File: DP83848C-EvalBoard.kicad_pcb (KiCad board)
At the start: 4 copper layers, 165 parts, among them J1 Conn_02x08_Odd_Even, J10 RJ45_LED_Shielded, J11 USB_C_Receptacle_USB2.0, J12 Conn_02x05_Odd_Even, J2 Conn_02x08_Odd_Even, J3 Conn_02x04_Odd_Even, J4 Conn_01x04, J5 Conn_01x04, J6 Conn_02x04_Odd_Even, J7 Conn_02x04_Odd_Even, J8 Conn_02x04_Odd_Even, J9 Conn_01x02, Q1 AO3401A, Q2 AO3400A, Q3 AO3401A, SW1 SW_Push, T1 H1102NL, U1 AMS1117-3.3, U2 DP83848C, U3 STM32F407VGTx, U4 USBLC6-2SC6, X1 50MHz, Y1 25MHz

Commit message: Test...
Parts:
- added R98: 0, Resistor_SMD:R_1206_3216Metric, F.Cu at (157.5, 40.6)
- added R99: 0, Resistor_SMD:R_1206_3216Metric, F.Cu at (157.5, 43.9)
- moved C14 10.4 mm to (139.7, 73.2), turned to 270 degrees
- moved R30 9.80 mm to (141.2, 78.2), turned to 270 degrees
- moved R25 9.51 mm to (141.2, 80.3), turned to 90 degrees
- moved C11 8.63 mm to (142.2, 78.2), turned to 90 degrees
- moved R26 8.29 mm to (142.2, 80.3), turned to 270 degrees
- moved R31 6.71 mm to (144.3, 78.2), turned to 270 degrees
- moved C12 5.85 mm to (143.3, 78.2), turned to 90 degrees
- moved R27 5.80 mm to (143.3, 80.3), turned to 90 degrees
- moved R28 5.39 mm to (144.3, 80.3), turned to 270 degrees
- moved C16 4.31 mm to (131.3, 57.7)
- moved J10 4.31 mm to (147.8, 51.3)
- moved R38 4.31 mm to (133.9, 61.5)
- moved R39 4.31 mm to (133.9, 60.2)
- moved R41 4.31 mm to (133.9, 57.7)
- moved T1 4.31 mm to (142.7, 66.5)
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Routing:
- net /PHY/RX+: track 17.7 -> 0.00 mm
- net /PHY/TX+: track 15.6 -> 0.00 mm
- net Net-(J10-Pad4): track 14.8 -> 0.00 mm
- net /PHY/RXC: track 14.2 -> 0.00 mm
- net /PHY/RX-: track 24.3 -> 11.8 mm
- net /PHY/TX-: track 10.8 -> 0.00 mm
- net /PHY/TXC: track 9.61 -> 0.00 mm
- net Net-(J10-Pad7): track 9.22 -> 0.00 mm
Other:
- board outline added: 105 x 150 mm
- net class Default: trace_width 0.25 -> 0.2; via_dia 0.8 -> 0.6; via_drill 0.4 -> 0.3

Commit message: Placement
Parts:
- added J13: Conn_01x04, Connector_PinHeader_2.54mm:PinHeader_1x04_P2.54mm_Vertical, F.Cu at (45.0, 132.2)
- added J14: Conn_02x04_Odd_Even, Connector_PinHeader_2.54mm:PinHeader_2x04_P2.54mm_Vertical, F.Cu at (121.9, 128.0)
- added R100: 33, Resistor_SMD:R_0805_2012Metric, F.Cu at (118.0, 128.0)
- added R101: 33, Resistor_SMD:R_0805_2012Metric, F.Cu at (118.0, 130.5)
- added R102: 33, Resistor_SMD:R_0805_2012Metric, F.Cu at (118.0, 133.0)
- added R103: 33, Resistor_SMD:R_0805_2012Metric, F.Cu at (118.0, 135.5)
- C10, C4: footprint Capacitor_SMD:C_0402_1005Metric -> Capacitor_Tantalum_SMD:CP_EIA-3216-18_Kemet-A
- R30, R31: value 0 -> 33; footprint Resistor_SMD:R_0402_1005Metric -> Resistor_SMD:R_0805_2012Metric
- R64, R65, R66, R67, R68, R69, R70, R71, R72, R73, R74, R75, R76, R77, R78, R79, R80, R81, R82, R83, R84, R85, R86, R87, R88, R89, R90, R91, R92, R93, R94, R95, R96, R97: footprint Resistor_SMD:R_1206_3216Metric -> Resistor_SMD:R_0805_2012Metric
- moved J7 202.2 mm to (47.9, 123.6), turned to 180 degrees
- moved R92 193.0 mm to (53.0, 123.6)
- moved R93 190.9 mm to (53.0, 121.1)
- moved R94 189.0 mm to (53.0, 118.5)
- moved R80 187.2 mm to (42.0, 101.5)
- moved R81 187.2 mm to (42.0, 104.1)
- moved R82 187.2 mm to (42.0, 106.6)
- moved R83 187.2 mm to (42.0, 109.1)
- moved R95 187.2 mm to (53.0, 116.0), turned to 0 degrees
- moved J2 186.8 mm to (46.9, 74.7)
- moved R72 186.8 mm to (41.8, 74.7)
- moved R73 186.8 mm to (41.8, 77.2)
- moved R74 186.8 mm to (41.8, 79.8)
- moved R75 186.8 mm to (41.8, 82.3)
- moved R76 186.8 mm to (41.8, 84.9)
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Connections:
- C11 pad 1: Net-(C11-Pad1) -> +3V3
- C12 pad 1: Net-(C12-Pad1) -> +3V3
- R25 pad 2: Net-(C11-Pad1) -> +3V3
- R26 pad 1: Net-(C11-Pad1) -> +3V3
- R27 pad 2: Net-(C12-Pad1) -> +3V3
- R28 pad 1: Net-(C12-Pad1) -> +3V3
- R30 pad 1: +3V3 -> /MCU/USART3_RX
- R30 pad 2: Net-(C11-Pad1) -> Net-(J13-Pad2)
- R31 pad 1: +3V3 -> /MCU/USART3_TX
- R31 pad 2: Net-(C12-Pad1) -> Net-(J13-Pad3)
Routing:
- net /PHY/TD-: track 0.00 -> 15.9 mm
- net /PHY/TD+: track 0.00 -> 15.8 mm
- net /PHY/RD-: track 0.00 -> 15.3 mm
- net /PHY/RD+: track 0.00 -> 14.2 mm
- net /PHY/PFB: track 0.00 -> 13.6 mm, vias 0 -> 2
- net /PHY/RX-: track 11.8 -> 0.00 mm
- net +3V3: track 0.00 -> 7.93 mm, vias 0 -> 7
- net Net-(R23-Pad2): track 0.00 -> 7.56 mm, vias 0 -> 2
- net GND: track 0.00 -> 5.69 mm, vias 0 -> 7
- net Net-(R24-Pad2): track 0.00 -> 5.44 mm, vias 0 -> 2
- net Net-(R19-Pad1): track 0.00 -> 4.58 mm
- net Net-(R16-Pad1): track 0.00 -> 4.47 mm
- net Net-(R18-Pad1): track 0.00 -> 4.43 mm
- net Net-(R14-Pad1): track 0.00 -> 4.35 mm
- net Net-(R10-Pad1): track 0.00 -> 4.24 mm
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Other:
- board size 105 x 150 mm -> 100 x 100 mm
- net class Default: clearance 0.2 -> 0.15; trace_width 0.2 -> 0.15
- rule trace_clearance: 0.2 -> 0.15
- rule trace_min: 0.2 -> 0.1
- rule via_min_drill: 0.3 -> 0.25
- rule via_min_size: 0.4 -> 0.5

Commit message: Routing
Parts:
- added C32: 10uF, Capacitor_Tantalum_SMD:CP_EIA-3216-18_Kemet-A, F.Cu at (88.8, 107.5)
- added H1: MountingHole_Pad, MountingHole:MountingHole_3.2mm_M3_Pad_Via, F.Cu at (45.0, 152.0)
- added H2: MountingHole_Pad, MountingHole:MountingHole_3.2mm_M3_Pad_Via, F.Cu at (45.0, 62.0)
- added H3: MountingHole_Pad, MountingHole:MountingHole_3.2mm_M3_Pad_Via, F.Cu at (120.0, 152.0)
- added H4: MountingHole_Pad, MountingHole:MountingHole_3.2mm_M3_Pad_Via, F.Cu at (120.0, 62.0)
- C1: footprint Capacitor_SMD:C_0402_1005Metric -> Capacitor_SMD:C_Elec_6.3x7.7
- C2: value 22uF -> 100uF; footprint Capacitor_SMD:C_0402_1005Metric -> Capacitor_Tantalum_SMD:CP_EIA-3528-15_AVX-H
- J10: footprint Connector_RJ:RJ45_Hanrun_HR911105A -> Connector_RJ:RJ45_Amphenol_RJHSE538X
- J9: footprint Connector_PinHeader_2.54mm:PinHeader_1x02_P2.54mm_Vertical -> ak:Molex_022112022
- R1, R2: footprint Resistor_SMD:R_0402_1005Metric -> Resistor_SMD:R_0603_1608Metric
- R100, R101, R102, R103, R30, R31, R64, R65, R66, R67, R68, R69, R70, R71, R72, R73, R74, R75, R76, R77, R78, R79, R80, R81, R82, R83, R84, R85, R86, R87, R88, R89, R90, R91, R92, R93, R94, R95, R96, R97: footprint Resistor_SMD:R_0805_2012Metric -> Resistor_SMD:R_0603_1608Metric
- moved J13 74.2 mm to (118.1, 144.8), turned to 180 degrees
- moved R30 61.2 mm to (109.2, 145.4), turned to 0 degrees
- moved R31 60.3 mm to (109.2, 139.7), turned to 0 degrees
- moved R56 59.3 mm to (97.0, 103.7)
- moved R54 56.7 mm to (99.2, 103.7)
- moved JP2 50.6 mm to (95.8, 67.0), turned to 0 degrees
- moved R34 50.3 mm to (98.8, 70.2), turned to 180 degrees
- moved R98 49.6 mm to (51.0, 66.0), turned to 180 degrees
- moved R36 46.7 mm to (74.0, 68.5), turned to 90 degrees
- moved R37 45.9 mm to (84.2, 68.5), turned to 90 degrees
- moved R35 45.8 mm to (98.8, 75.2), turned to 180 degrees
- moved J10 45.1 mm to (49.0, 81.0), turned to 90 degrees
- moved R55 45.0 mm to (97.0, 114.0)
- moved JP7 44.9 mm to (99.3, 111.2), turned to 180 degrees
- moved C4 44.1 mm to (92.0, 69.8), turned to 90 degrees
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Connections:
- net /ADC0 renamed /MCU/ADC_IN0
- net /ADC1 renamed /MCU/ADC_IN3
- net /ADC2 renamed /MCU/ADC_IN6
- net /ADC3 renamed /MCU/ADC_IN8
- net /ADC4 renamed /MCU/ADC_IN9
- net /ADC5 renamed /MCU/ADC_IN10
- net /ADC6 renamed /MCU/ADC_IN12
- net /ADC7 renamed /MCU/ADC_IN13
- net /GPIO0 renamed /MCU/GPIO0
- net /GPIO1 renamed /MCU/GPIO1
- net /GPIO2 renamed /MCU/GPIO2
- net /GPIO3 renamed /MCU/GPIO3
- net /GPIO4 renamed /MCU/GPIO4
- net /GPIO5 renamed /MCU/GPIO5
- net /GPIO6 renamed /MCU/GPIO6
- net /GPIO7 renamed /MCU/GPIO7
- net /TMR1 renamed /MCU/TMR_CH1
- net /TMR2 renamed /MCU/TMR_CH2
- net /TMR3 renamed /MCU/TMR_CH3
- net /TMR4 renamed /MCU/TMR_CH4
- net Net-(J1-Pad1) renamed /GPIO0_R
- net Net-(J1-Pad11) renamed /GPIO5_R
- net Net-(J1-Pad13) renamed /GPIO6_R
- net Net-(J1-Pad15) renamed /GPIO7_R
- net Net-(J1-Pad3) renamed /GPIO1_R
- net Net-(J1-Pad5) renamed /GPIO2_R
- net Net-(J1-Pad7) renamed /GPIO3_R
- net Net-(J1-Pad9) renamed /GPIO4_R
- net Net-(J13-Pad2) renamed /USART3_TX_R
- net Net-(J13-Pad3) renamed /USART3_RX_R
- net Net-(J14-Pad1) renamed /SPI3_MISO_R
- net Net-(J14-Pad3) renamed /SPI3_MOSI_R
- net Net-(J14-Pad5) renamed /SPI3_SCK_R
- net Net-(J14-Pad7) renamed /SPI3_NSS_R
- net Net-(J2-Pad1) renamed /ADC0_R
- net Net-(J2-Pad11) renamed /ADC5_R
- net Net-(J2-Pad13) renamed /ADC6_R
- net Net-(J2-Pad15) renamed /ADC7_R
- net Net-(J2-Pad3) renamed /ADC1_R
- net Net-(J2-Pad5) renamed /ADC2_R
- net Net-(J2-Pad7) renamed /ADC3_R
- net Net-(J2-Pad9) renamed /ADC4_R
- net Net-(J3-Pad1) renamed /TMR1_R
- net Net-(J3-Pad3) renamed /TMR2_R
- net Net-(J3-Pad5) renamed /TMR3_R
- net Net-(J3-Pad7) renamed /TMR4_R
- net Net-(J4-Pad2) renamed /USART1_TX_R
- net Net-(J4-Pad3) renamed /USART1_RX_R
- net Net-(J5-Pad2) renamed /USART2_TX_R
- net Net-(J5-Pad3) renamed /USART2_RX_R
- net Net-(J6-Pad1) renamed /SPI1_MISO_R
- net Net-(J6-Pad3) renamed /SPI1_MOSI_R
- net Net-(J6-Pad5) renamed /SPI1_SCK_R
- net Net-(J6-Pad7) renamed /SPI1_NSS
- net Net-(J7-Pad1) renamed /SPI2_MISO_R
- net Net-(J7-Pad3) renamed /SPI2_MOSI_R
- net Net-(J7-Pad5) renamed /SPI2_SCK_R
- net Net-(J7-Pad7) renamed /SPI2_NSS_R
- net Net-(R51-Pad1) renamed /MCU/VREF+
- J8 pad 2: +3V3 -> Net-(J8-Pad2)
- J8 pad 3: Net-(J8-Pad3) -> /I2C1_SCL_R
- J8 pad 4: Net-(J8-Pad4) -> /I2C1_SCL_R
- J8 pad 5: Net-(J8-Pad5) -> /I2C1_SDA_R
- J8 pad 6: Net-(J8-Pad6) -> /I2C1_SDA_R
- J8 pad 8: +3V3 -> Net-(J8-Pad8)
- R1 pad 1: Net-(J8-Pad6) -> +3V3
- R1 pad 2: Net-(J8-Pad5) -> Net-(J8-Pad2)
- R2 pad 1: Net-(J8-Pad4) -> +3V3
- R2 pad 2: Net-(J8-Pad3) -> Net-(J8-Pad8)
- R30 pad 1: /MCU/USART3_RX -> /MCU/USART3_TX
- R31 pad 1: /MCU/USART3_TX -> /MCU/USART3_RX
- R84 pad 1: /USART1_RX -> /MCU/USART1_TX
- R85 pad 1: /USART1_TX -> /MCU/USART1_RX
- R86 pad 1: /USART2_RX -> /MCU/USART2_TX
- R87 pad 1: /USART2_TX -> /MCU/USART2_RX
- R96 pad 1: Net-(J8-Pad3) -> /I2C1_SCL_R
- R96 pad 2: /MCU/I2C1_SDA -> /MCU/I2C1_SCL
- R97 pad 1: Net-(J8-Pad5) -> /I2C1_SDA_R
- R97 pad 2: /MCU/I2C1_SCL -> /MCU/I2C1_SDA
- U3 pad 68: /USART1_TX -> /MCU/USART1_TX
- U3 pad 69: /USART1_RX -> /MCU/USART1_RX
- U3 pad 86: /USART2_TX -> /MCU/USART2_TX
- U3 pad 87: /USART2_RX -> /MCU/USART2_RX
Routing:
- net /MCU/NRST: track 0.00 -> 92.5 mm, vias 0 -> 2
- net /ETH_TX_D1: track 0.00 -> 67.3 mm, vias 0 -> 1
- net /ETH_TX_D0: track 0.00 -> 66.4 mm, vias 0 -> 2
- net /ETH_TX_EN: track 0.00 -> 66.0 mm, vias 0 -> 2
- net /ETH_RXD1: track 0.00 -> 58.2 mm, vias 0 -> 2
- net /ETH_RXD0: track 0.00 -> 56.4 mm, vias 0 -> 2
- net /ETH_CRS_DV: track 0.00 -> 53.8 mm, vias 0 -> 2
- net /MCU/USART2_TX: track 0.00 -> 50.4 mm, vias 0 -> 2
- net /MCU/GPIO6: track 0.00 -> 47.8 mm
- net /MCU/USART3_RX: track 0.00 -> 47.5 mm, vias 0 -> 2
- net /MCU/GPIO5: track 0.00 -> 46.2 mm
- net /MCU/SPI2_NSS: track 0.00 -> 45.6 mm, vias 0 -> 2
- net /MCU/USART3_TX: track 0.00 -> 45.6 mm, vias 0 -> 2
- net /MCU/GPIO4: track 0.00 -> 44.0 mm
- net /MCU/USART2_RX: track 0.00 -> 43.7 mm, vias 0 -> 2
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- added copper zone on In2.Cu, net +3V3
- added copper zone on In1.Cu, net GND
- added copper zone on F.Cu, net GNDPWR
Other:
- board size 100 x 100 mm -> 85 x 100 mm
- board text added: "1"
- board text added: "2"
- board text added: "3"
- board text added: "3V3"
- board text added: "4k7 pull-up"
- board text added: "AN0"
- board text added: "AN1"
- board text added: "AN2"
- board text added: "AN3"
- board text added: "AN4"
- board text added: "AN5"
- board text added: "AN6"
- board text added: "AN7"
- board text added: "ANALOG"
- board text added: "GND"
- board text added: "GPIO"
- board text added: "GROUND"
- board text added: "I2C"
- board text added: "MISO"
- board text added: "MOSI"
- board text added: "PE0"
- board text added: "PE1"
- board text added: "PE2"
- board text added: "PE3"
- board text added: "PE4"
- board text added: "PE5"
- board text added: "PE6"
- board text added: "PE7"
- board text added: "RX"
- board text added: "SCK"
- board text added: "SCL"
- board text added: "SDA"
- board text added: "SPI1"
- board text added: "SPI2"
- board text added: "SPI3"
- board text added: "TIMER"
- board text added: "TMR1"
- board text added: "TMR2"
- board text added: "TMR3"
- board text added: "TMR4"
- board text added: "TX"
- board text added: "USART"
- board text added: "~SS"

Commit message: Layout
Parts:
- moved R34 25.4 mm to (75.2, 60.8), turned to 270 degrees
- moved C19 25.2 mm to (87.0, 147.2), turned to 0 degrees
- moved D1 23.7 mm to (46.1, 145.5), turned to 90 degrees
- moved R35 23.5 mm to (80.2, 60.8), turned to 270 degrees
- moved R3 22.1 mm to (47.6, 145.5), turned to 90 degrees
- moved R63 22.0 mm to (89.0, 146.0)
- moved JP2 20.7 mm to (75.2, 64.2), turned to 90 degrees
- moved J9 17.6 mm to (52.2, 150.8)
- moved R62 13.8 mm to (92.2, 146.0)
- moved R4 13.5 mm to (61.8, 133.2), turned to 90 degrees
- moved SW1 12.9 mm to (80.0, 150.0), turned to 0 degrees
- moved R103 12.7 mm to (99.7, 130.8)
- moved Q1 12.6 mm to (60.5, 136.8)
- moved Q3 12.6 mm to (64.2, 136.8)
- moved F1 12.4 mm to (68.8, 142.5), turned to 270 degrees
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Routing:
- net /MCU/NRST: track 92.5 -> 3.66 mm, vias 2 -> 0
- net /ETH_TX_D1: track 67.3 -> 0.00 mm, vias 1 -> 0
- net /ETH_TX_D0: track 66.4 -> 0.00 mm, vias 2 -> 0
- net /MCU/GPIO7: track 0.00 -> 66.0 mm, vias 0 -> 2
- net /ETH_TX_EN: track 66.0 -> 0.00 mm, vias 2 -> 0
- net /ETH_RXD1: track 58.2 -> 0.00 mm, vias 2 -> 0
- net /ETH_RXD0: track 56.4 -> 0.00 mm, vias 2 -> 0
- net /ETH_CRS_DV: track 53.8 -> 0.00 mm, vias 2 -> 0
- net /MCU/SPI1_NSS: track 41.7 -> 0.00 mm, vias 2 -> 0
- net /MCU/SPI1_SCK: track 41.3 -> 0.00 mm, vias 2 -> 0
- net /MCU/ADC_IN10: track 31.2 -> 0.00 mm, vias 2 -> 0
- net /MCU/BOOT1: track 30.8 -> 0.00 mm, vias 2 -> 0
- net /MCU/ADC_IN12: track 29.6 -> 0.00 mm, vias 2 -> 0
- net /MCU/ADC_IN13: track 27.3 -> 0.00 mm, vias 2 -> 0
- net /ETH_MDIO: track 37.8 -> 10.6 mm
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- added copper zone on F.Cu, net +3V3
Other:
- board size 85 x 100 mm -> 75 x 100 mm
- net class Default: clearance 0.15 -> 0.2; trace_width 0.15 -> 0.2
- net class Power added: clearance 0.2, trace_width 0.3, via_dia 0.6, via_drill 0.3
- rule trace_clearance: 0.15 -> 0.2
- board text added: "5V"
- board text added: "RESET"
- board text added: "ST-LINK"

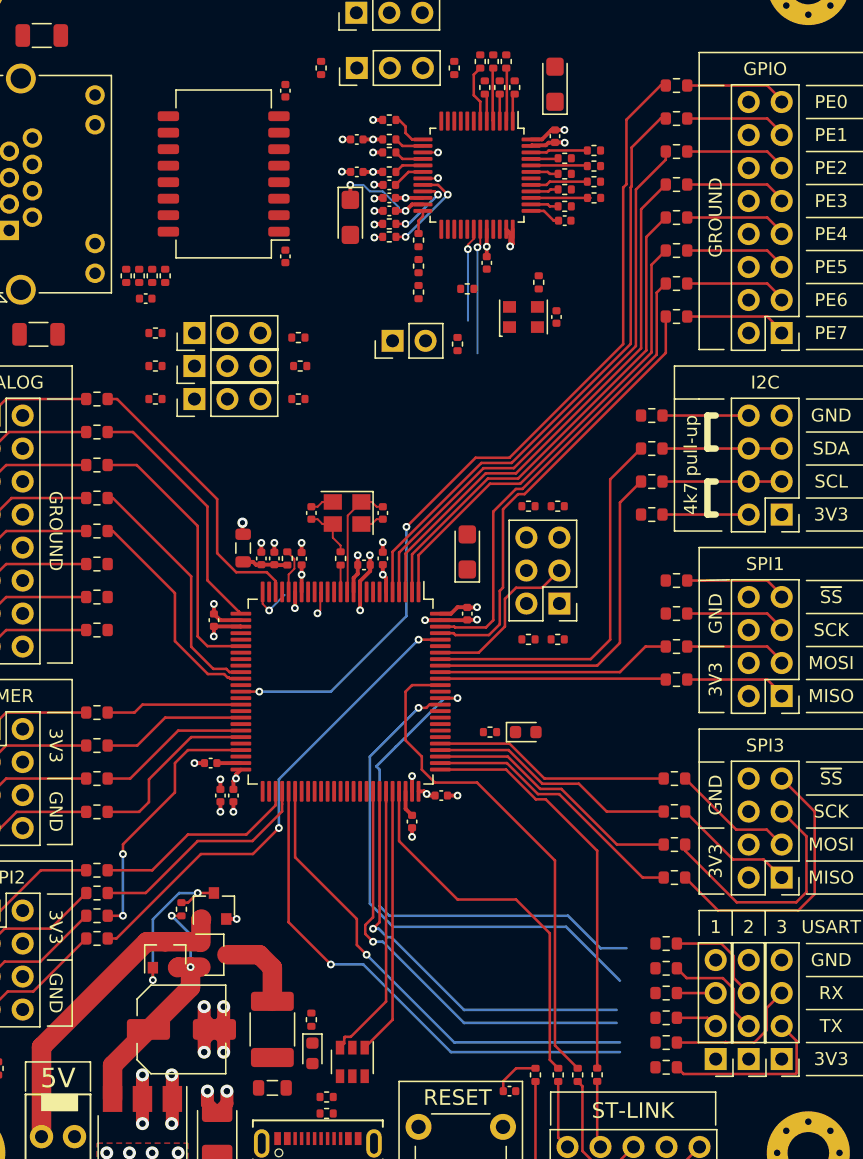
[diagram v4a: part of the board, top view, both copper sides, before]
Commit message: Added ESD protection
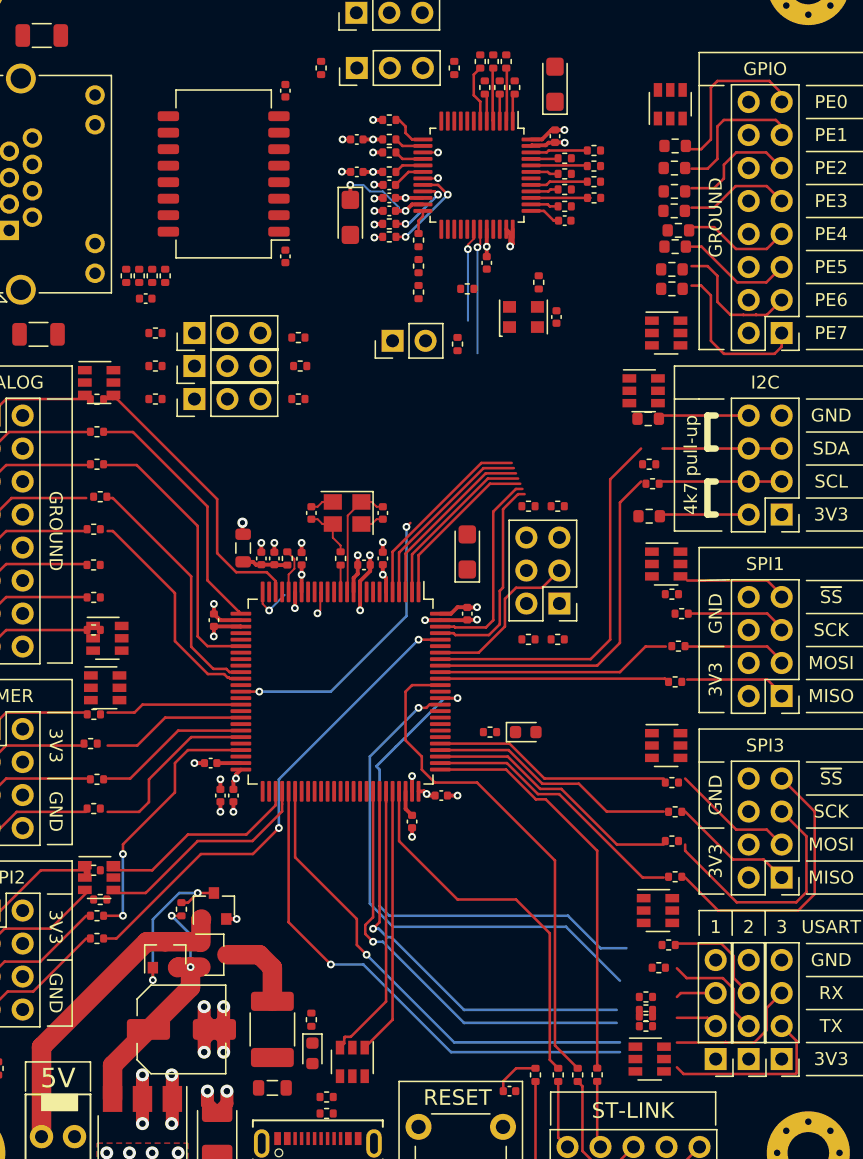
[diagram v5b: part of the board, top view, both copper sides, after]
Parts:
- removed the J1 at (108.0, 88.9)
- removed the J2 at (47.0, 95.2)
- removed the J3 at (47.0, 119.4)
- removed the J4 at (102.9, 144.8)
- removed the R1 at (98.0, 102.9)
- removed the R2 at (98.0, 95.2)
- removed the R30 at (99.1, 145.4)
- removed the R31 at (99.1, 143.5)
- added J10: Conn_02x04_Odd_Even, Connector_PinHeader_2.54mm:PinHeader_2x04_P2.54mm_Vertical, F.Cu at (47.0, 119.4)
- added J11: Conn_02x04_Odd_Even, Connector_PinHeader_2.54mm:PinHeader_2x04_P2.54mm_Vertical, F.Cu at (108.0, 116.8)
- added J12: Conn_02x04_Odd_Even, Connector_PinHeader_2.54mm:PinHeader_2x04_P2.54mm_Vertical, F.Cu at (47.0, 133.3)
- added J9: Conn_02x08_Odd_Even, Connector_PinHeader_2.54mm:PinHeader_2x08_P2.54mm_Vertical, F.Cu at (47.0, 95.2)
- added R62: 33, Resistor_SMD:R_0603_1608Metric, F.Cu at (99.5, 85.5)
- added R63: 33, Resistor_SMD:R_0603_1608Metric, F.Cu at (99.5, 84.0)
- added R98: 33, Resistor_SMD:R_0402_1005Metric, F.Cu at (97.5, 141.0)
- added R99: 33, Resistor_SMD:R_0402_1005Metric, F.Cu at (97.5, 142.2)
- added U10: CM1224, Package_TO_SOT_SMD:SOT-23-6, F.Cu at (97.8, 144.8)
- added U11: CM1224, Package_TO_SOT_SMD:SOT-23-6, F.Cu at (55.4, 92.7)
- added U12: CM1224, Package_TO_SOT_SMD:SOT-23-6, F.Cu at (99.1, 120.7)
- added U13: CM1224, Package_TO_SOT_SMD:SOT-23-6, F.Cu at (97.3, 93.3)
- added U14: CM1224, Package_TO_SOT_SMD:SOT-23-6, F.Cu at (55.9, 116.2)
- added U15: CM1224, Package_TO_SOT_SMD:SOT-23-6, F.Cu at (56.0, 112.4)
- added U5: CM1224, Package_TO_SOT_SMD:SOT-23-6, F.Cu at (99.1, 88.9)
- added U6: CM1224, Package_TO_SOT_SMD:SOT-23-6, F.Cu at (99.1, 106.7)
- added U7: CM1224, Package_TO_SOT_SMD:SOT-23-6, F.Cu at (98.4, 133.3)
- added U8: CM1224, Package_TO_SOT_SMD:SOT-23-6, F.Cu at (99.4, 71.3)
- added U9: CM1224, Package_TO_SOT_SMD:SOT-23-6, F.Cu at (55.4, 130.8)
- J13: value Conn_01x04 -> Conn_02x04_Odd_Even; footprint Connector_PinHeader_2.54mm:PinHeader_1x04_P2.54mm_Vertical -> Connector_PinHeader_2.54mm:PinHeader_2x04_P2.54mm_Vertical
- J6, J7: value Conn_02x04_Odd_Even -> Conn_01x04; footprint Connector_PinHeader_2.54mm:PinHeader_2x04_P2.54mm_Vertical -> Connector_PinHeader_2.54mm:PinHeader_1x04_P2.54mm_Vertical
- J8: value Conn_02x04_Odd_Even -> Conn_02x08_Odd_Even; footprint Connector_PinHeader_2.54mm:PinHeader_2x04_P2.54mm_Vertical -> Connector_PinHeader_2.54mm:PinHeader_2x08_P2.54mm_Vertical
- R1: renamed from R3; value 220 -> 33
- R100, R101: value 33 -> 4k7
- R102, R103, R70, R71, R72, R73, R74, R75, R76, R77, R78, R79, R80, R81, R82, R83, R84, R85, R86, R87, R88, R89, R90, R91, R92, R93, R94, R95, R96, R97: footprint Resistor_SMD:R_0603_1608Metric -> Resistor_SMD:R_0402_1005Metric
- R3: renamed from R5; value 220 -> 33
- R42: renamed from R44; value 220 -> 33
- R45: renamed from R47; value 220 -> 33
- R46: renamed from R48; value 220 -> 33
- moved J7 62.0 mm to (108.0, 144.8), turned to 180 degrees
- moved R71 52.0 mm to (55.2, 96.5), turned to 180 degrees
- moved R89 49.9 mm to (55.2, 135.5), turned to 0 degrees
- moved R70 49.6 mm to (55.2, 94.0), turned to 180 degrees
- moved R88 48.2 mm to (55.2, 133.8), turned to 0 degrees
- moved R83 46.5 mm to (100.0, 113.0)
- moved R82 45.1 mm to (99.8, 115.8)
- moved R86 44.7 mm to (55.0, 130.2)
- moved R93 44.5 mm to (99.8, 130.8), turned to 180 degrees
- moved R92 44.3 mm to (99.5, 128.0), turned to 180 degrees
- moved R87 43.7 mm to (55.5, 132.5)
- moved R94 43.0 mm to (97.5, 141.5)
- moved R95 42.5 mm to (97.5, 140.0)
- moved R97 38.2 mm to (99.2, 136.0), turned to 0 degrees
- moved R96 37.4 mm to (98.5, 137.8), turned to 0 degrees
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- renumbered C32 to C17, C17 to C19, C19 to C20, C20 to C22, C22 to C23, C23 to C24, C24 to C25, C25 to C26, C26 to C27, C27 to C28, C28 to C29, C29 to C30, C30 to C31, C31 to C32, J9 to J1, J10 to J2, J11 to J3, J12 to J4, R12 to R10, R13 to R11, R14 to R12, R15 to R13, R16 to R14, R17 to R15, R18 to R16, R19 to R17, R20 to R18, R21 to R19, R4 to R2, R22 to R20, R23 to R21, R24 to R22, R25 to R23, R26 to R24, R27 to R25, R28 to R26, R29 to R27, R32 to R28, R33 to R29, R34 to R30, R35 to R31, R36 to R32, R37 to R33, R38 to R34, R39 to R35, R40 to R36, R41 to R37, R42 to R38, R43 to R39, R6 to R4, R98 to R40, R99 to R41, R45 to R43, R46 to R44, R49 to R47, R50 to R48, R51 to R49, R7 to R5, R52 to R50, R53 to R51, R54 to R52, R55 to R53, R56 to R54, R57 to R55, R58 to R56, R59 to R57, R60 to R58, R61 to R59, R8 to R6, R62 to R60, R63 to R61, R9 to R7, R10 to R8, R11 to R9
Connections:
- J13 pad 1: +3V3 -> /IO/SPI3_MISO_R
- J13 pad 2: /USART3_TX_R -> +3V3
- J13 pad 3: /USART3_RX_R -> /IO/SPI3_MOSI_R
- J13 pad 4: GND -> +3V3
- J14 pad 1: /SPI3_MISO_R -> +3V3
- J14 pad 2: +3V3 -> Net-(J14-Pad2)
- J14 pad 3: /SPI3_MOSI_R -> /IO/I2C1_SCL_R
- J14 pad 4: +3V3 -> /IO/I2C1_SCL_R
- J14 pad 5: /SPI3_SCK_R -> /IO/I2C1_SDA_R
- J14 pad 6: GND -> /IO/I2C1_SDA_R
- J14 pad 7: /SPI3_NSS_R -> GND
- J14 pad 8: GND -> Net-(J14-Pad8)
- J5 pad 2: /USART2_TX_R -> /IO/USART1_TX_R
- J5 pad 3: /USART2_RX_R -> /IO/USART1_RX_R
- J6 pad 1: /SPI1_MISO_R -> +3V3
- J6 pad 2: +3V3 -> /IO/USART2_TX_R
- J6 pad 3: /SPI1_MOSI_R -> /IO/USART2_RX_R
- J6 pad 4: +3V3 -> GND
- J7 pad 1: /SPI2_MISO_R -> +3V3
- J7 pad 2: +3V3 -> /IO/USART3_TX_R
- J7 pad 3: /SPI2_MOSI_R -> /IO/USART3_RX_R
- J7 pad 4: +3V3 -> GND
- J8 pad 1: +3V3 -> /IO/GPIO0_R
- J8 pad 2: Net-(J8-Pad2) -> GND
- J8 pad 3: /I2C1_SCL_R -> /IO/GPIO1_R
- J8 pad 4: /I2C1_SCL_R -> GND
- J8 pad 5: /I2C1_SDA_R -> /IO/GPIO2_R
- J8 pad 6: /I2C1_SDA_R -> GND
- J8 pad 7: GND -> /IO/GPIO3_R
- J8 pad 8: Net-(J8-Pad8) -> GND
- R100 pad 1: /SPI3_MISO_R -> +3V3
- R100 pad 2: /MCU/SPI3_MISO -> Net-(J14-Pad2)
- R101 pad 1: /SPI3_MOSI_R -> +3V3
- R101 pad 2: /MCU/SPI3_MOSI -> Net-(J14-Pad8)
- R102 pad 1: /SPI3_SCK_R -> /IO/I2C1_SCL_R
- R102 pad 2: /MCU/SPI3_SCK -> /IO/I2C1_SCL
- R103 pad 1: /SPI3_NSS_R -> /IO/I2C1_SDA_R
- R103 pad 2: /MCU/SPI3_NSS -> /IO/I2C1_SDA
- R64 pad 1: /MCU/GPIO0 -> /IO/GPIO2
- R64 pad 2: /GPIO0_R -> /IO/GPIO2_R
- R65 pad 1: /MCU/GPIO1 -> /IO/GPIO3
- R65 pad 2: /GPIO1_R -> /IO/GPIO3_R
- R66 pad 1: /MCU/GPIO2 -> /IO/GPIO4
- R66 pad 2: /GPIO2_R -> /IO/GPIO4_R
- R67 pad 1: /MCU/GPIO3 -> /IO/GPIO5
- R67 pad 2: /GPIO3_R -> /IO/GPIO5_R
- R68 pad 1: /MCU/GPIO4 -> /IO/GPIO6
- R68 pad 2: /GPIO4_R -> /IO/GPIO6_R
- R69 pad 1: /MCU/GPIO5 -> /IO/GPIO7
- R69 pad 2: /GPIO5_R -> /IO/GPIO7_R
- R70 pad 1: /MCU/GPIO6 -> /IO/ADC0
- R70 pad 2: /GPIO6_R -> /IO/ADC0_R
- R71 pad 1: /MCU/GPIO7 -> /IO/ADC1
- R71 pad 2: /GPIO7_R -> /IO/ADC1_R
- R72 pad 1: /MCU/ADC_IN0 -> /IO/ADC2
- R72 pad 2: /ADC0_R -> /IO/ADC2_R
- R73 pad 1: /MCU/ADC_IN3 -> /IO/ADC3
- R73 pad 2: /ADC1_R -> /IO/ADC3_R
- R74 pad 1: /MCU/ADC_IN6 -> /IO/ADC4
- R74 pad 2: /ADC2_R -> /IO/ADC4_R
- R75 pad 1: /MCU/ADC_IN8 -> /IO/ADC5
- R75 pad 2: /ADC3_R -> /IO/ADC5_R
- R76 pad 1: /MCU/ADC_IN9 -> /IO/ADC6
- R76 pad 2: /ADC4_R -> /IO/ADC6_R
- R77 pad 1: /MCU/ADC_IN10 -> /IO/ADC7
- R77 pad 2: /ADC5_R -> /IO/ADC7_R
- R78 pad 1: /MCU/ADC_IN12 -> /IO/TMR1
- R78 pad 2: /ADC6_R -> /IO/TMR1_R
- R79 pad 1: /MCU/ADC_IN13 -> /IO/TMR2
- R79 pad 2: /ADC7_R -> /IO/TMR2_R
- R80 pad 1: /MCU/TMR_CH1 -> /IO/TMR3
- R80 pad 2: /TMR1_R -> /IO/TMR3_R
- R81 pad 1: /MCU/TMR_CH2 -> /IO/TMR4
- R81 pad 2: /TMR2_R -> /IO/TMR4_R
- R82 pad 1: /MCU/TMR_CH3 -> /IO/SPI1_MISO_R
- R82 pad 2: /TMR3_R -> /IO/SPI1_MISO
- R83 pad 1: /MCU/TMR_CH4 -> /IO/SPI1_MOSI_R
- R83 pad 2: /TMR4_R -> /IO/SPI1_MOSI
- R84 pad 1: /MCU/USART1_TX -> /IO/SPI1_SCK_R
- R84 pad 2: /USART1_TX_R -> /IO/SPI1_SCK
- R85 pad 1: /MCU/USART1_RX -> /IO/SPI1_NSS
- R85 pad 2: /USART1_RX_R -> /IO/SPI1_NSS
- R86 pad 1: /MCU/USART2_TX -> /IO/SPI2_MISO_R
- R86 pad 2: /USART2_TX_R -> /IO/SPI2_MISO
- R87 pad 1: /MCU/USART2_RX -> /IO/SPI2_MOSI_R
- R87 pad 2: /USART2_RX_R -> /IO/SPI2_MOSI
- R88 pad 1: /SPI1_MISO_R -> /IO/SPI2_SCK_R
- R88 pad 2: /MCU/SPI1_MISO -> /IO/SPI2_SCK
- R89 pad 1: /SPI1_MOSI_R -> /IO/SPI2_NSS_R
- R89 pad 2: /MCU/SPI1_MOSI -> /IO/SPI2_NSS
- R90 pad 1: /SPI1_SCK_R -> /IO/SPI3_MISO_R
- R90 pad 2: /MCU/SPI1_SCK -> /IO/SPI3_MISO
- R91 pad 1: /SPI1_NSS -> /IO/SPI3_MOSI_R
- R91 pad 2: /MCU/SPI1_NSS -> /IO/SPI3_MOSI
- R92 pad 1: /SPI2_MISO_R -> /IO/SPI3_SCK_R
- R92 pad 2: /MCU/SPI2_MISO -> /IO/SPI3_SCK
- R93 pad 1: /SPI2_MOSI_R -> /IO/SPI3_NSS_R
- R93 pad 2: /MCU/SPI2_MOSI -> /IO/SPI3_NSS
- R94 pad 1: /SPI2_SCK_R -> /IO/USART1_TX
- R94 pad 2: /MCU/SPI2_SCK -> /IO/USART1_TX_R
- R95 pad 1: /SPI2_NSS_R -> /IO/USART1_RX
- R95 pad 2: /MCU/SPI2_NSS -> /IO/USART1_RX_R
- R96 pad 1: /I2C1_SCL_R -> /IO/USART2_TX
- R96 pad 2: /MCU/I2C1_SCL -> /IO/USART2_TX_R
- R97 pad 1: /I2C1_SDA_R -> /IO/USART2_RX
- R97 pad 2: /MCU/I2C1_SDA -> /IO/USART2_RX_R
- U3 pad 1: /MCU/GPIO2 -> /IO/GPIO2
- U3 pad 15: /MCU/ADC_IN10 -> /IO/ADC5
- U3 pad 17: /MCU/ADC_IN12 -> /IO/ADC6
- U3 pad 18: /MCU/ADC_IN13 -> /IO/ADC7
- U3 pad 2: /MCU/GPIO3 -> /IO/GPIO3
- U3 pad 23: /MCU/ADC_IN0 -> /IO/ADC0
- U3 pad 26: /MCU/ADC_IN3 -> /IO/ADC1
- U3 pad 29: /MCU/SPI1_NSS -> /IO/SPI1_NSS
- U3 pad 3: /MCU/GPIO4 -> /IO/GPIO4
- U3 pad 30: /MCU/SPI1_SCK -> /IO/SPI1_SCK
- U3 pad 31: /MCU/ADC_IN6 -> /IO/ADC2
- U3 pad 35: /MCU/ADC_IN8 -> /IO/ADC3
- U3 pad 36: /MCU/ADC_IN9 -> /IO/ADC4
- U3 pad 38: /MCU/GPIO7 -> /IO/GPIO7
- U3 pad 4: /MCU/GPIO5 -> /IO/GPIO5
- U3 pad 40: /MCU/TMR_CH1 -> /IO/TMR1
- U3 pad 42: /MCU/TMR_CH2 -> /IO/TMR2
- U3 pad 44: /MCU/TMR_CH3 -> /IO/TMR3
- U3 pad 45: /MCU/TMR_CH4 -> /IO/TMR4
- U3 pad 47: /MCU/SPI2_SCK -> /IO/SPI2_SCK
- U3 pad 5: /MCU/GPIO6 -> /IO/GPIO6
- U3 pad 53: /MCU/SPI2_MISO -> /IO/SPI2_MISO
- U3 pad 54: /MCU/SPI2_MOSI -> /IO/SPI2_MOSI
- U3 pad 55: /MCU/USART3_TX -> /IO/USART3_TX
- U3 pad 56: /MCU/USART3_RX -> /IO/USART3_RX
- U3 pad 68: /MCU/USART1_TX -> /IO/USART1_TX
- U3 pad 69: /MCU/USART1_RX -> /IO/USART1_RX
- U3 pad 77: /MCU/SPI3_NSS -> /IO/SPI3_NSS
- U3 pad 78: /MCU/SPI3_SCK -> /IO/SPI3_SCK
- U3 pad 79: /MCU/SPI3_MISO -> /IO/SPI3_MISO
- U3 pad 80: /MCU/SPI3_MOSI -> /IO/SPI3_MOSI
- U3 pad 86: /MCU/USART2_TX -> /IO/USART2_TX
- U3 pad 87: /MCU/USART2_RX -> /IO/USART2_RX
- U3 pad 90: /MCU/SPI1_MISO -> /IO/SPI1_MISO
- U3 pad 91: /MCU/SPI1_MOSI -> /IO/SPI1_MOSI
- U3 pad 92: /MCU/I2C1_SCL -> /IO/I2C1_SCL
- U3 pad 93: /MCU/I2C1_SDA -> /IO/I2C1_SDA
- U3 pad 96: /MCU/SPI2_NSS -> /IO/SPI2_NSS
- U3 pad 97: /MCU/GPIO0 -> /IO/GPIO0
- U3 pad 98: /MCU/GPIO1 -> /IO/GPIO1
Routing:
- net /MCU/GPIO7: track 66.0 -> 0.00 mm, vias 2 -> 0
- net /MCU/GPIO6: track 46.7 -> 0.00 mm
- net /MCU/GPIO5: track 43.8 -> 0.00 mm
- net /MCU/GPIO4: track 41.0 -> 0.00 mm
- net /MCU/USART2_RX: track 40.9 -> 0.00 mm, vias 1 -> 0
- net /IO/USART2_RX: track 0.00 -> 40.9 mm, vias 0 -> 1
- net /MCU/USART2_TX: track 40.1 -> 0.00 mm, vias 1 -> 0
- net /IO/USART2_TX: track 0.00 -> 40.1 mm, vias 0 -> 1
- net /MCU/USART3_TX: track 39.7 -> 0.00 mm, vias 1 -> 0
- net /IO/USART3_TX: track 0.00 -> 39.7 mm, vias 0 -> 1
- net /MCU/GPIO3: track 38.3 -> 0.00 mm
- net /MCU/SPI2_NSS: track 37.3 -> 0.00 mm, vias 2 -> 0
- net /IO/SPI2_NSS: track 0.00 -> 37.3 mm, vias 0 -> 2
- net /MCU/USART3_RX: track 37.1 -> 0.00 mm, vias 1 -> 0
- net /IO/USART3_RX: track 0.00 -> 37.1 mm, vias 0 -> 1
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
